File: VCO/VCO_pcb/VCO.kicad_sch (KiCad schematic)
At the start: 66 parts, among them J1 Thonkiconn, J2 Thonkiconn, J3 Thonkiconn, J4 Thonkiconn, J5 Thonkiconn, Q1 BCM847BS,115, Q2 MMBFJ111, U1 TL074, U2 TL074, U3 TL072

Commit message: adds schematic page comments
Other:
- company: (none) -> www.solisynth.com
- title: (none) -> VCO
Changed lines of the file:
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@@
 (kicad_sch (version 20211123) (generator eeschema)
   (paper "A3")
+  (title_block
+    (title "VCO")
+    (date "2023-01-21")
+    (rev "1")
+    (company "www.solisynth.com")
+  )
   (junction (at 118.11 210.82) (diameter 0) (color 0 0 0 0)
   )

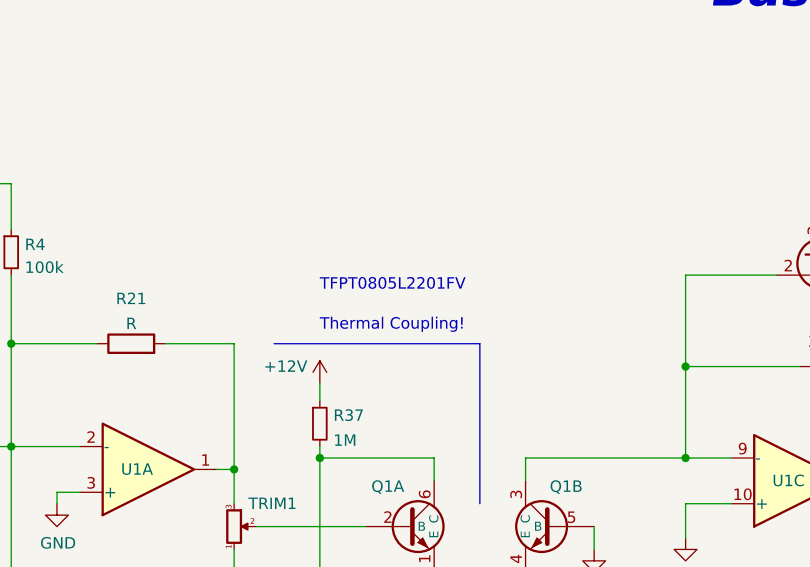
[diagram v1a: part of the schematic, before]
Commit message: removes wrong partnumber of PTC thermistor
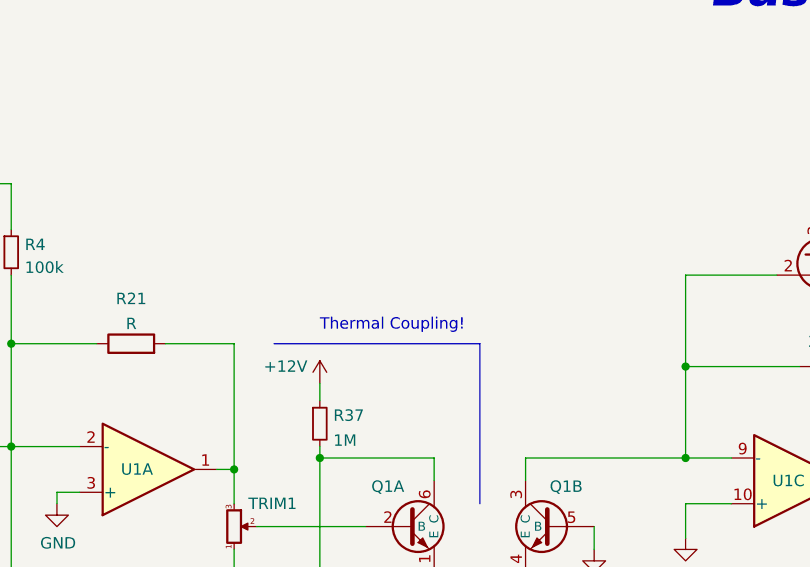
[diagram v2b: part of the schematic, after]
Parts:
- D3, D4: MFN (none) -> Panjit International Inc.; MPN (none) -> SBA130AS_R1_00001
- Q1: Arrow Part Number BCM847BS,115 -> (none); Arrow Price/Stock https://www.arrow.com/en/products/bcm847bs115/nexperia -> (none); MFN (none) -> Nexperia; MPN (none) -> BCM847BS,115; Manufacturer_Name Nexperia -> (none); Manufacturer_Part_Number BCM847BS,115 -> (none); Mouser Part Number 771-BCM847BS-T/R -> (none); Mouser Price/Stock https://www.mouser.co.uk/ProductDetail/Nexperia/BCM847BS115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 -> (none)
- R21: MFN (none) -> Vishay / Dale; MPN (none) -> TFPTL15L2201JL2B
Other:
- note removed: "TFPT0805L2201FV"
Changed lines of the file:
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@@
-    (effects (font (size 1.27 1.27)) (justify left bottom))
-  )
-  (text "TFPT0805L2201FV" (at 95.25 73.66 0)
     (effects (font (size 1.27 1.27)) (justify left bottom))
   )
@@
       (effects (font (size 1.27 1.27)) hide)
     )
+    (property "MFN" "Panjit International Inc." (id 4) (at 125.73 205.74 0)
+      (effects (font (size 1.27 1.27)) hide)
+    )
+    (property "MPN" "SBA130AS_R1_00001" (id 5) (at 125.73 205.74 0)
+      (effects (font (size 1.27 1.27)) hide)
+    )
     (pin "1")
     (pin "2")
@@
     )
     (property "Datasheet" "~" (id 3) (at 125.73 215.9 0)
+      (effects (font (size 1.27 1.27)) hide)
+    )
+    (property "MFN" "Panjit International Inc." (id 4) (at 125.73 215.9 0)
+      (effects (font (size 1.27 1.27)) hide)
+    )
+    (property "MPN" "SBA130AS_R1_00001" (id 5) (at 125.73 215.9 0)
       (effects (font (size 1.27 1.27)) hide)
     )
@@
       (effects (font (size 1.27 1.27)) (justify left) hide)
     )
-    (property "Manufacturer_Name" "Nexperia" (id 6) (at 93.98 107.315 0)
-      (effects (font (size 1.27 1.27)) (justify left) hide)
-    )
-    (property "Manufacturer_Part_Number" "BCM847BS,115" (id 7) (at 93.98 109.855 0)
-      (effects (font (size 1.27 1.27)) (justify left) hide)
-    )
-    (property "Arrow Part Number" "BCM847BS,115" (id 8) (at 93.98 112.395 0)
-      (effects (font (size 1.27 1.27)) (justify left) hide)
-    )
-    (property "Arrow Price/Stock" "https://www.arrow.com/en/products/bcm847bs115/nexperia" (id 9) (at 93.98 114.935 0)
-      (effects (font (size 1.27 1.27)) (justify left) hide)
-    )
-    (property "Mouser Part Number" "771-BCM847BS-T/R" (id 10) (at 93.98 117.475 0)
-      (effects (font (size 1.27 1.27)) (justify left) hide)
-    )
-    (property "Mouser Price/Stock" "https://www.mouser.co.uk/ProductDetail/Nexperia/BCM847BS115?qs=me8TqzrmIYUrX4V%252Bwao%2FgQ%3D%3D" (id 11) (at 93.98 120.015 0)
-      (effects (font (size 1.27 1.27)) (justify left) hide)
+    (property "MFN" "Nexperia" (id 6) (at 120.65 99.695 0)
+      (effects (font (size 1.27 1.27)) hide)
+    )
+    (property "MPN" "BCM847BS,115" (id 7) (at 120.65 99.695 0)
+      (effects (font (size 1.27 1.27)) hide)
     )
     (pin "1")
@@
       (effects (font (size 1.27 1.27)) hide)
     )
-    (property "Datasheet" "~" (id 3) (at 74.295 79.375 0)
+    (property "Datasheet" "https://www.mouser.de/datasheet/2/427/tfptl-1762894.pdf" (id 3) (at 74.295 79.375 0)
+      (effects (font (size 1.27 1.27)) hide)
+    )
+    (property "MFN" "Vishay / Dale" (id 4) (at 74.295 79.375 0)
+      (effects (font (size 1.27 1.27)) hide)
+    )
+    (property "MPN" "TFPTL15L2201JL2B" (id 5) (at 74.295 79.375 0)
       (effects (font (size 1.27 1.27)) hide)
     )
@@
       (effects (font (size 1.27 1.27)) (justify left) hide)
     )
-    (property "Manufacturer_Name" "Nexperia" (id 6) (at 132.08 107.315 0)
-      (effects (font (size 1.27 1.27)) (justify left) hide)
-    )
-    (property "Manufacturer_Part_Number" "BCM847BS,115" (id 7) (at 132.08 109.855 0)
-      (effects (font (size 1.27 1.27)) (justify left) hide)
-    )
-    (property "Arrow Part Number" "BCM847BS,115" (id 8) (at 132.08 112.395 0)
-      (effects (font (size 1.27 1.27)) (justify left) hide)
-    )
-    (property "Arrow Price/Stock" "https://www.arrow.com/en/products/bcm847bs115/nexperia" (id 9) (at 132.08 114.935 0)
-      (effects (font (size 1.27 1.27)) (justify left) hide)
-    )
-    (property "Mouser Part Number" "771-BCM847BS-T/R" (id 10) (at 132.08 117.475 0)
-      (effects (font (size 1.27 1.27)) (justify left) hide)
-    )
-    (property "Mouser Price/Stock" "https://www.mouser.co.uk/ProductDetail/Nexperia/BCM847BS115?qs=me8TqzrmIYUrX4V%252Bwao%2FgQ%3D%3D" (id 11) (at 132.08 120.015 0)
-      (effects (font (size 1.27 1.27)) (justify left) hide)
-    )
-    (pin "1")
+    (property "MFN" "Nexperia" (id 6) (at 105.41 99.695 0)
+      (effects (font (size 1.27 1.27)) hide)
+    )
+    (property "MPN" "BCM847BS,115" (id 7) (at 105.41 99.695 0)
+      (effects (font (size 1.27 1.27)) hide)
+    )
+    (pin "1")

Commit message: changing all diodes to same type
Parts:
- D1, D2, D5: value 1N5819HW-7-F -> D; MFN Diodes Incorporated -> Panjit International Inc.; MPN 1N5819HW-7-F -> SBA130AS_R1_00001
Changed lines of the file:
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@@
       (effects (font (size 1.27 1.27)) (justify right))
     )
-    (property "Value" "1N5819HW-7-F" (id 1) (at 297.307 119.9766 90)
+    (property "Value" "D" (id 1) (at 297.307 119.9766 90)
       (effects (font (size 1.27 1.27)) (justify right) hide)
     )
@@
       (effects (font (size 1.27 1.27)) hide)
     )
-    (property "MFN" "Diodes Incorporated" (id 4) (at 292.735 118.11 0)
-      (effects (font (size 1.27 1.27)) hide)
-    )
-    (property "MPN" "1N5819HW-7-F" (id 5) (at 292.735 118.11 0)
+    (property "MFN" "Panjit International Inc." (id 4) (at 292.735 118.11 0)
+      (effects (font (size 1.27 1.27)) hide)
+    )
+    (property "MPN" "SBA130AS_R1_00001" (id 5) (at 292.735 118.11 0)
       (effects (font (size 1.27 1.27)) hide)
     )
@@
       (effects (font (size 1.27 1.27)) (justify right))
     )
-    (property "Value" "1N5819HW-7-F" (id 1) (at 233.807 121.8816 90)
+    (property "Value" "D" (id 1) (at 233.807 121.8816 90)
       (effects (font (size 1.27 1.27)) (justify right) hide)
     )
@@
       (effects (font (size 1.27 1.27)) hide)
     )
-    (property "MFN" "Diodes Incorporated" (id 4) (at 229.235 120.015 0)
-      (effects (font (size 1.27 1.27)) hide)
-    )
-    (property "MPN" "1N5819HW-7-F" (id 5) (at 229.235 120.015 0)
+    (property "MFN" "Panjit International Inc." (id 4) (at 229.235 120.015 0)
+      (effects (font (size 1.27 1.27)) hide)
+    )
+    (property "MPN" "SBA130AS_R1_00001" (id 5) (at 229.235 120.015 0)
       (effects (font (size 1.27 1.27)) hide)
     )
@@
       (effects (font (size 1.27 1.27)) (justify right))
     )
-    (property "Value" "1N5819HW-7-F" (id 1) (at 160.655 135.255 90)
+    (property "Value" "D" (id 1) (at 160.655 135.255 90)
       (effects (font (size 1.27 1.27)) (justify right) hide)
     )
@@
       (effects (font (size 1.27 1.27)) hide)
     )
-    (property "MFN" "Diodes Incorporated" (id 4) (at 179.07 125.73 0)
-      (effects (font (size 1.27 1.27)) hide)
-    )
-    (property "MPN" "1N5819HW-7-F" (id 5) (at 179.07 125.73 0)
+    (property "MFN" "Panjit International Inc." (id 4) (at 179.07 125.73 0)
+      (effects (font (size 1.27 1.27)) hide)
+    )
+    (property "MPN" "SBA130AS_R1_00001" (id 5) (at 179.07 125.73 0)
       (effects (font (size 1.27 1.27)) hide)
     )
@@
     )
     (path "/680aac74-6a36-4423-a0aa-b7a684e36c21"
-      (reference "D1") (unit 1) (value "1N5819HW-7-F") (footprint "ic_packages:SOD-123")
+      (reference "D1") (unit 1) (value "D") (footprint "ic_packages:SOD-123")
     )
     (path "/0dc7e8dc-d373-4344-8471-49b0ac457e22"
-      (reference "D2") (unit 1) (value "1N5819HW-7-F") (footprint "ic_packages:SOD-123")
+      (reference "D2") (unit 1) (value "D") (footprint "ic_packages:SOD-123")
     )
     (path "/00000000-0000-0000-0000-00006009e9f7"
@@
     )
     (path "/f4877c20-d0ed-485d-8283-1a850da29526"
-      (reference "D5") (unit 1) (value "1N5819HW-7-F") (footprint "ic_packages:SOD-123")
+      (reference "D5") (unit 1) (value "D") (footprint "ic_packages:SOD-123")
     )
     (path "/fd54b468-c7e8-426a-a4eb-1ff17d22227a"

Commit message: consolidating 20k res
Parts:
- R17: MPN CR0603FX2002ELF -> CR0603-FX-2002ELF
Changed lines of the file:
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@@
       (effects (font (size 1.27 1.27)) hide)
     )
-    (property "MPN" "CR0603FX2002ELF" (id 5) (at 205.74 112.395 0)
+    (property "MPN" "CR0603-FX-2002ELF" (id 5) (at 205.74 112.395 0)
       (effects (font (size 1.27 1.27)) hide)
     )

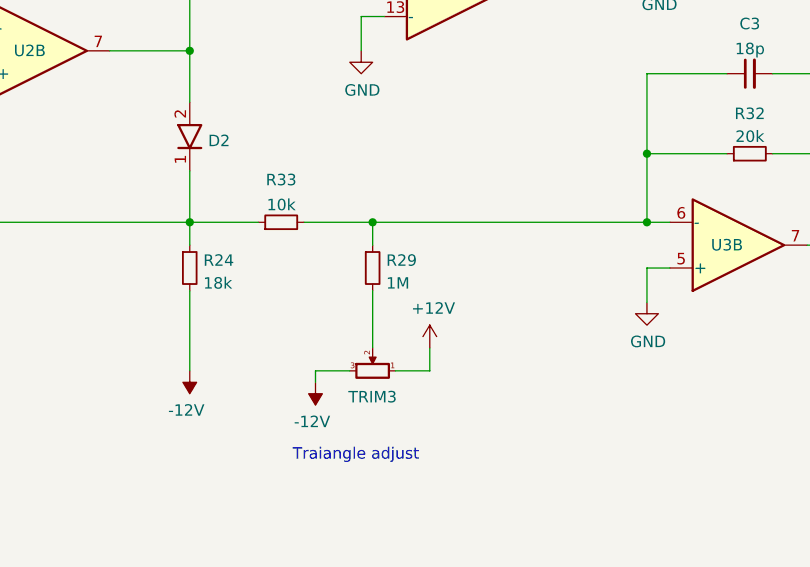
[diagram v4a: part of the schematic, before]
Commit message: chaging 1M to 30k for triangle adjustment
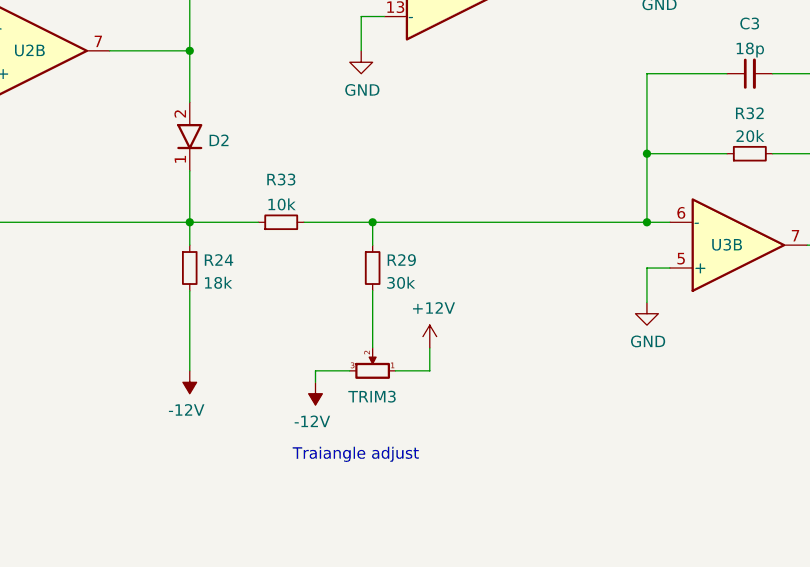
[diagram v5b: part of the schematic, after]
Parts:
- removed R29: 1M, passive_parts:R_0603_1608Metric, symbol resistor_0603:1M
- added R29: 30k, passive_parts:R_0603_1608Metric, symbol resistor_0603:30k
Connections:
- net at C3.1, R32.1, R33.2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: now also R29.1
- net at TRIM3.2: now also R29.2
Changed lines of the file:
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@@
+    (pin "2")
+  )
+  (symbol (lib_id "resistor_0603:30k") (at 315.595 132.715 0) (unit 1)
+    (in_bom yes) (on_board yes) (fields_autoplaced)
+    (property "Reference" "R29" (id 0) (at 317.0936 131.8803 0)
+      (effects (font (size 1.27 1.27)) (justify left))
+    )
+    (property "Value" "30k" (id 1) (at 317.0936 134.4172 0)
+      (effects (font (size 1.27 1.27)) (justify left))
+    )
+    (property "Footprint" "passive_parts:R_0603_1608Metric" (id 2) (at 339.725 112.395 0)
+      (effects (font (size 1.27 1.27)) hide)
+    )
+    (property "Datasheet" "https://www.bourns.com/docs/product-datasheets/cr.pdf?sfvrsn=574d41f6_14" (id 3) (at 324.485 116.205 0)
+      (effects (font (size 1.27 1.27)) (justify left) hide)
+    )
+    (property "MFN" "Bourns" (id 4) (at 324.485 118.745 0)
+      (effects (font (size 1.27 1.27)) (justify left) hide)
+    )
+    (property "MPN" "CR0603-FX-3002ELF" (id 5) (at 324.485 121.285 0)
+      (effects (font (size 1.27 1.27)) (justify left) hide)
+    )
+    (property "Tolerance" "1%" (id 6) (at 324.485 123.825 0)
+      (effects (font (size 1.27 1.27)) (justify left) hide)
+    )
+    (property "Power" "~" (id 7) (at 324.485 126.365 0)
+      (effects (font (size 1.27 1.27)) (justify left) hide)
+    )
+    (property "LCSC" "~" (id 8) (at 324.485 128.905 0)
+      (effects (font (size 1.27 1.27)) (justify left) hide)
+    )
+    (pin "1")
     (pin "2")
   )
@@
     (pin "2")
   )
-  (symbol (lib_id "resistor_0603:1M") (at 315.595 132.715 0) (unit 1)
-    (in_bom yes) (on_board yes) (fields_autoplaced)
-    (property "Reference" "R29" (id 0) (at 317.0936 131.8803 0)
-      (effects (font (size 1.27 1.27)) (justify left))
-    )
-    (property "Value" "1M" (id 1) (at 317.0936 134.4172 0)
-      (effects (font (size 1.27 1.27)) (justify left))
-    )
-    (property "Footprint" "passive_parts:R_0603_1608Metric" (id 2) (at 339.725 112.395 0)
-      (effects (font (size 1.27 1.27)) hide)
-    )
-    (property "Datasheet" "https://www.bourns.com/docs/product-datasheets/cr.pdf?sfvrsn=574d41f6_14" (id 3) (at 324.485 116.205 0)
-      (effects (font (size 1.27 1.27)) (justify left) hide)
-    )
-    (property "MFN" "Bourns" (id 4) (at 324.485 118.745 0)
-      (effects (font (size 1.27 1.27)) (justify left) hide)
-    )
-    (property "MPN" "CR0603-FX-1004ELF" (id 5) (at 324.485 121.285 0)
-      (effects (font (size 1.27 1.27)) (justify left) hide)
-    )
-    (property "Tolerance" "1%" (id 6) (at 324.485 123.825 0)
-      (effects (font (size 1.27 1.27)) (justify left) hide)
-    )
-    (property "Power" "1/10W" (id 7) (at 324.485 126.365 0)
-      (effects (font (size 1.27 1.27)) (justify left) hide)
-    )
-    (property "LCSC" "~" (id 8) (at 324.485 128.905 0)
-      (effects (font (size 1.27 1.27)) (justify left) hide)
-    )
-    (pin "1")
-    (pin "2")
-  )
   (symbol (lib_id "connectors:PINHEADER_02x05") (at 106.68 220.98 0) (unit 1)
     (in_bom yes) (on_board yes)
@@
       (reference "R28") (unit 1) (value "20k") (footprint "passive_parts:R_0603_1608Metric")
     )
-    (path "/fb4ff6fb-6ca5-416b-93f8-7f735695c5f7"
-      (reference "R29") (unit 1) (value "1M") (footprint "passive_parts:R_0603_1608Metric")
+    (path "/2568de00-863f-4670-b272-2de2636f3fd4"
+      (reference "R29") (unit 1) (value "30k") (footprint "passive_parts:R_0603_1608Metric")
     )
     (path "/ba5450e1-31c8-4fb6-8102-18f804efc884"

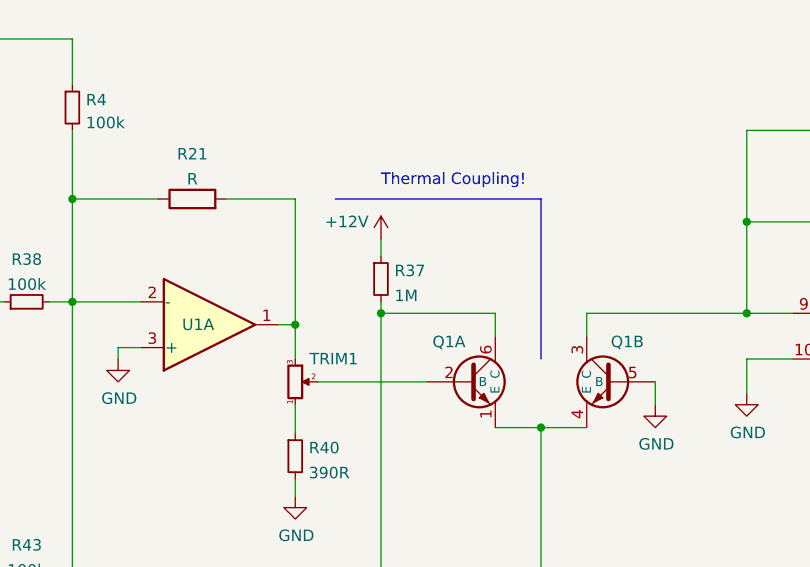
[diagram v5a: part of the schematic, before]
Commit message: changing R37 from 1M to 2M2 to get lower minimal frequency
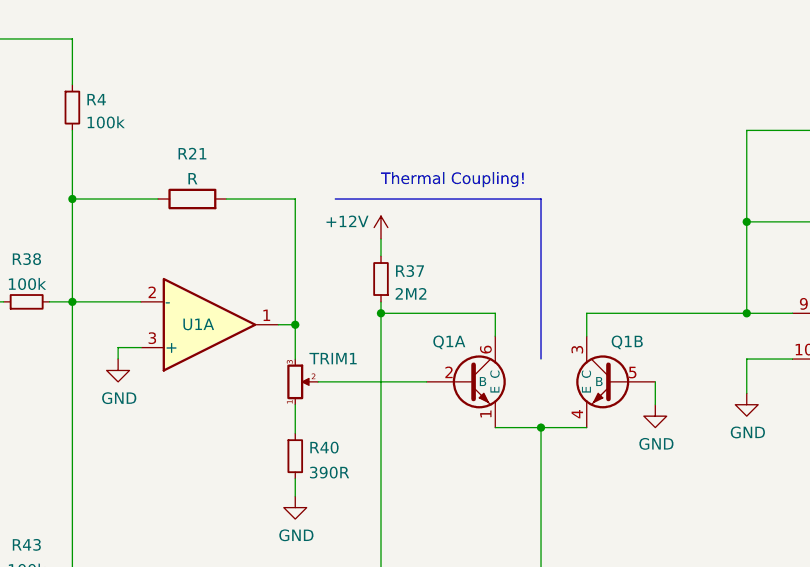
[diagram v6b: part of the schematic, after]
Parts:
- removed R37: 1M, passive_parts:R_0603_1608Metric, symbol resistor_0603:1M
- added R37: 2M2, passive_parts:R_0603_1608Metric, symbol resistor_0603:2M2
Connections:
- net +12V: now also R37.2
- net at C5.1, Q1.6 (C), R46.2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: now also R37.1
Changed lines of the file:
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@@
+    (pin "2")
+  )
+  (symbol (lib_id "resistor_0603:2M2") (at 95.25 88.265 180) (unit 1)
+    (in_bom yes) (on_board yes) (fields_autoplaced)
+    (property "Reference" "R37" (id 0) (at 96.7486 87.4303 0)
+      (effects (font (size 1.27 1.27)) (justify right))
+    )
+    (property "Value" "2M2" (id 1) (at 96.7486 89.9672 0)
+      (effects (font (size 1.27 1.27)) (justify right))
+    )
+    (property "Footprint" "passive_parts:R_0603_1608Metric" (id 2) (at 71.12 108.585 0)
+      (effects (font (size 1.27 1.27)) hide)
+    )
+    (property "Datasheet" "https://www.yageo.com/upload/media/product/productsearch/datasheet/rchip/PYu-RC_Group_51_RoHS_L_12.pdf" (id 3) (at 86.36 104.775 0)
+      (effects (font (size 1.27 1.27)) (justify left) hide)
+    )
+    (property "MFN" "Yageo" (id 4) (at 86.36 102.235 0)
+      (effects (font (size 1.27 1.27)) (justify left) hide)
+    )
+    (property "MPN" "RC0603FR-132M2L" (id 5) (at 86.36 99.695 0)
+      (effects (font (size 1.27 1.27)) (justify left) hide)
+    )
+    (property "Tolerance" "1%" (id 6) (at 86.36 97.155 0)
+      (effects (font (size 1.27 1.27)) (justify left) hide)
+    )
+    (property "Power" "1/10W" (id 7) (at 86.36 94.615 0)
+      (effects (font (size 1.27 1.27)) (justify left) hide)
+    )
+    (property "LCSC" "~" (id 8) (at 86.36 92.075 0)
+      (effects (font (size 1.27 1.27)) (justify left) hide)
+    )
+    (pin "1")
     (pin "2")
   )
@@
     (pin "1")
   )
-  (symbol (lib_id "resistor_0603:1M") (at 95.25 88.265 0) (unit 1)
-    (in_bom yes) (on_board yes) (fields_autoplaced)
-    (property "Reference" "R37" (id 0) (at 96.7486 87.3565 0)
-      (effects (font (size 1.27 1.27)) (justify left))
-    )
-    (property "Value" "1M" (id 1) (at 96.7486 90.1316 0)
-      (effects (font (size 1.27 1.27)) (justify left))
-    )
-    (property "Footprint" "passive_parts:R_0603_1608Metric" (id 2) (at 119.38 67.945 0)
-      (effects (font (size 1.27 1.27)) hide)
-    )
-    (property "Datasheet" "https://www.bourns.com/docs/product-datasheets/cr.pdf?sfvrsn=574d41f6_14" (id 3) (at 104.14 71.755 0)
-      (effects (font (size 1.27 1.27)) (justify left) hide)
-    )
-    (property "MFN" "Bourns" (id 4) (at 104.14 74.295 0)
-      (effects (font (size 1.27 1.27)) (justify left) hide)
-    )
-    (property "MPN" "CR0603-FX-1004ELF" (id 5) (at 104.14 76.835 0)
-      (effects (font (size 1.27 1.27)) (justify left) hide)
-    )
-    (property "Tolerance" "1%" (id 6) (at 104.14 79.375 0)
-      (effects (font (size 1.27 1.27)) (justify left) hide)
-    )
-    (property "Power" "1/10W" (id 7) (at 104.14 81.915 0)
-      (effects (font (size 1.27 1.27)) (justify left) hide)
-    )
-    (property "LCSC" "~" (id 8) (at 104.14 84.455 0)
-      (effects (font (size 1.27 1.27)) (justify left) hide)
-    )
-    (pin "1")
-    (pin "2")
-  )
   (symbol (lib_id "capacitor_mlcc_0603:100n") (at 194.31 207.01 0) (unit 1)
     (in_bom yes) (on_board yes) (fields_autoplaced)
@@
       (reference "R36") (unit 1) (value "1k") (footprint "passive_parts:R_0603_1608Metric")
     )
-    (path "/b1d8368c-eeed-4e52-8591-9c8198ae6721"
-      (reference "R37") (unit 1) (value "1M") (footprint "passive_parts:R_0603_1608Metric")
+    (path "/4e7ad0e3-9de8-4b55-b80a-02c2d08ad493"
+      (reference "R37") (unit 1) (value "2M2") (footprint "passive_parts:R_0603_1608Metric")
     )
     (path "/2cdae8a7-eccb-4a27-89c9-a8cc21e134d8"
